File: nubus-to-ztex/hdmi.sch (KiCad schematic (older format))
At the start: 7 parts, among them J5 HDMI_A, U5 TPD12S016PWR

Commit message: large update
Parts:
- U5: URL (none) -> https://lcsc.com/product-detail/Interface-Specialized_Texas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
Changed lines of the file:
@@
 $Descr A4 11693 8268
 encoding utf-8
-Sheet 5 7
+Sheet 4 7
 Title "sbus-to-ztex blinkey stuff"
 Date ""
@@
 F 7 "IPC 7351B" H 3300 2700 50  0001 L BNN "STANDARD"
 F 8 "TPD12S016PWR" H 3300 2700 50  0001 C CNN "MPN"
+F 9 "https://lcsc.com/product-detail/Interface-Specialized_Texas-Instruments-TPD12S016PWR_C201665.html" H 3300 2700 50  0001 C CNN "URL"
 	1    3300 2700
 	1    0    0    -1

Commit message: large clean-up update
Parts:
- renumbered C21 to C20, C8 to C21, C4 to C22, C6 to C23, C7 to C24, U5 to U9
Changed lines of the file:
@@
 encoding utf-8
 Sheet 4 7
-Title "sbus-to-ztex blinkey stuff"
+Title "nubus-to-ztex HDMI"
 Date ""
 Rev ""
@@
 $EndDescr
 $Comp
-L TPD12S016PWR:TPD12S016PWR U5
+L TPD12S016PWR:TPD12S016PWR U9
 U 1 1 6148D344
 P 3300 2700
-F 0 "U5" H 3300 4067 50  0000 C CNN
+F 0 "U9" H 3300 4067 50  0000 C CNN
 F 1 "TPD12S016PWR" H 3300 3976 50  0000 C CNN
 F 2 "For_SeeedStudio:SOP65P640X120-24N" H 3300 2700 50  0001 L BNN
@@
 	4000 3800 4000 3900
 $Comp
-L power:GND #PWR0111
+L power:GND #PWR099
 U 1 1 60DDF342
 P 4000 3900
-F 0 "#PWR0111" H 4000 3650 50  0001 C CNN
+F 0 "#PWR099" H 4000 3650 50  0001 C CNN
 F 1 "GND" H 4005 3727 50  0000 C CNN
 F 2 "" H 4000 3900 50  0001 C CNN
@@
 P 4650 1300
 AR Path="/5F679B53/6148D345" Ref="C?"  Part="1"
-AR Path="/5F6B165A/6148D345" Ref="C7"  Part="1"
-AR Path="/612D28DD/6148D345" Ref="C18"  Part="1"
-AR Path="/61B62C00/6148D345" Ref="C15"  Part="1"
-F 0 "C15" H 4675 1400 50  0000 L CNN
+AR Path="/5F6B165A/6148D345" Ref="C?"  Part="1"
+AR Path="/612D28DD/6148D345" Ref="C?"  Part="1"
+AR Path="/61B62C00/6148D345" Ref="C24"  Part="1"
+F 0 "C24" H 4675 1400 50  0000 L CNN
 F 1 "100nF" H 4675 1200 50  0000 L CNN
 F 2 "Capacitor_SMD:C_0603_1608Metric" H 4688 1150 50  0001 C CNN
@@
 $EndComp
 $Comp
-L power:GND #PWR0112
+L power:GND #PWR0100
 U 1 1 6148D346
 P 4650 1450
-F 0 "#PWR0112" H 4650 1200 50  0001 C CNN
+F 0 "#PWR0100" H 4650 1200 50  0001 C CNN
 F 1 "GND" H 4655 1277 50  0000 C CNN
 F 2 "" H 4650 1450 50  0001 C CNN
@@
 $EndComp
 $Comp
-L power:+3V3 #PWR0113
+L power:+3V3 #PWR097
 U 1 1 6148D347
 P 2600 1600
-F 0 "#PWR0113" H 2600 1450 50  0001 C CNN
+F 0 "#PWR097" H 2600 1450 50  0001 C CNN
 F 1 "+3V3" H 2615 1773 50  0000 C CNN
 F 2 "" H 2600 1600 50  0001 C CNN
@@
 $EndComp
 $Comp
-L power:+5V #PWR0173
+L power:+5V #PWR098
 U 1 1 6148D348
 P 2600 1900
-F 0 "#PWR0173" H 2600 1750 50  0001 C CNN
+F 0 "#PWR098" H 2600 1750 50  0001 C CNN
 F 1 "+5V" H 2615 2073 50  0000 C CNN
 F 2 "" H 2600 1900 50  0001 C CNN
@@
 P 2250 1600
 AR Path="/5F679B53/6148D349" Ref="C?"  Part="1"
-AR Path="/5F6B165A/6148D349" Ref="C4"  Part="1"
-AR Path="/612D28DD/6148D349" Ref="C16"  Part="1"
-AR Path="/61B62C00/6148D349" Ref="C13"  Part="1"
-F 0 "C13" H 2275 1700 50  0000 L CNN
+AR Path="/5F6B165A/6148D349" Ref="C?"  Part="1"
+AR Path="/612D28DD/6148D349" Ref="C?"  Part="1"
+AR Path="/61B62C00/6148D349" Ref="C22"  Part="1"
+F 0 "C22" H 2275 1700 50  0000 L CNN
 F 1 "100nF" H 2275 1500 50  0000 L CNN
 F 2 "Capacitor_SMD:C_0603_1608Metric" H 2288 1450 50  0001 C CNN
@@
 $EndComp
 $Comp
-L power:GND #PWR0174
+L power:GND #PWR096
 U 1 1 6148D34A
 P 2100 1600
-F 0 "#PWR0174" H 2100 1350 50  0001 C CNN
+F 0 "#PWR096" H 2100 1350 50  0001 C CNN
 F 1 "GND" V 2105 1472 50  0000 R CNN
 F 2 "" H 2100 1600 50  0001 C CNN
@@
 P 2450 1900
 AR Path="/5F679B53/6148D34B" Ref="C?"  Part="1"
-AR Path="/5F6B165A/6148D34B" Ref="C6"  Part="1"
-AR Path="/612D28DD/6148D34B" Ref="C17"  Part="1"
-AR Path="/61B62C00/6148D34B" Ref="C14"  Part="1"
-F 0 "C14" H 2475 2000 50  0000 L CNN
+AR Path="/5F6B165A/6148D34B" Ref="C?"  Part="1"
+AR Path="/612D28DD/6148D34B" Ref="C?"  Part="1"
+AR Path="/61B62C00/6148D34B" Ref="C23"  Part="1"
+F 0 "C23" H 2475 2000 50  0000 L CNN
 F 1 "100nF" H 2475 1800 50  0000 L CNN
 F 2 "Capacitor_SMD:C_0603_1608Metric" H 2488 1750 50  0001 C CNN
@@
 P 2250 1350
 AR Path="/5F69F4EF/6148D34D" Ref="C?"  Part="1"
-AR Path="/5F6B165A/6148D34D" Ref="C8"  Part="1"
-AR Path="/612D28DD/6148D34D" Ref="C15"  Part="1"
-AR Path="/61B62C00/6148D34D" Ref="C12"  Part="1"
-F 0 "C12" H 2275 1450 50  0000 L CNN
+AR Path="/5F6B165A/6148D34D" Ref="C?"  Part="1"
+AR Path="/612D28DD/6148D34D" Ref="C?"  Part="1"
+AR Path="/61B62C00/6148D34D" Ref="C21"  Part="1"
+F 0 "C21" H 2275 1450 50  0000 L CNN
 F 1 "47uF 10V+" H 2275 1250 50  0000 L CNN
 F 2 "Capacitor_SMD:C_0805_2012Metric" H 2288 1200 50  0001 C CNN
@@
 AR Path="/5F6B165A/61B9B186" Ref="C?"  Part="1"
 AR Path="/612D28DD/61B9B186" Ref="C?"  Part="1"
-AR Path="/61B62C00/61B9B186" Ref="C21"  Part="1"
-F 0 "C21" H 2275 1200 50  0000 L CNN
+AR Path="/61B62C00/61B9B186" Ref="C20"  Part="1"
+F 0 "C20" H 2275 1200 50  0000 L CNN
 F 1 "10nF" H 2275 1000 50  0000 L CNN
 F 2 "Capacitor_SMD:C_0603_1608Metric" H 2288 950 50  0001 C CNN

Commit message: some missing stuff, minor HW update, SW
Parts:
- J5: URL https://www2.mouser.com/ProductDetail/Amphenol-FCI/10029449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 -> https://lcsc.com/product-detail/D-Sub-DVI-HDMI-Connectors_A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; URL-ALT (none) -> https://www2.mouser.com/ProductDetail/Amphenol-FCI/10029449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
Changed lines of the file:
@@
 F 3 "https://en.wikipedia.org/wiki/HDMI" H 6675 2550 50  0001 C CNN
 F 4 "10029449-111" H 6650 2550 50  0001 C CNN "MPN"
-F 5 "https://www2.mouser.com/ProductDetail/Amphenol-FCI/10029449-111RLF?qs=fmpTyLOWOey0HPdD9%2F%2FaXA%3D%3D" H 6650 2550 50  0001 C CNN "URL"
+F 5 "https://www2.mouser.com/ProductDetail/Amphenol-FCI/10029449-111RLF?qs=fmpTyLOWOey0HPdD9%2F%2FaXA%3D%3D" H 6650 2550 50  0001 C CNN "URL-ALT"
+F 6 "https://lcsc.com/product-detail/D-Sub-DVI-HDMI-Connectors_Amphenol-ICC-10029449-111RLF_C427307.html" H 6650 2550 50  0001 C CNN "URL"
 	1    6650 2550
 	1    0    0    -1

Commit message: cleanups, alternative MPN for 2x32 headers (TBC)
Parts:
- J5: MPN 10029449-111 -> 10029449-111RLF
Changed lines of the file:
@@
 F 2 "For_SeeedStudio:HDMI_A_Amphenol_10029449-111" H 6675 2550 50  0001 C CNN
 F 3 "https://en.wikipedia.org/wiki/HDMI" H 6675 2550 50  0001 C CNN
-F 4 "10029449-111" H 6650 2550 50  0001 C CNN "MPN"
+F 4 "10029449-111RLF" H 6650 2550 50  0001 C CNN "MPN"
 F 5 "https://www2.mouser.com/ProductDetail/Amphenol-FCI/10029449-111RLF?qs=fmpTyLOWOey0HPdD9%2F%2FaXA%3D%3D" H 6650 2550 50  0001 C CNN "URL-ALT"
 F 6 "https://lcsc.com/product-detail/D-Sub-DVI-HDMI-Connectors_Amphenol-ICC-10029449-111RLF_C427307.html" H 6650 2550 50  0001 C CNN "URL"

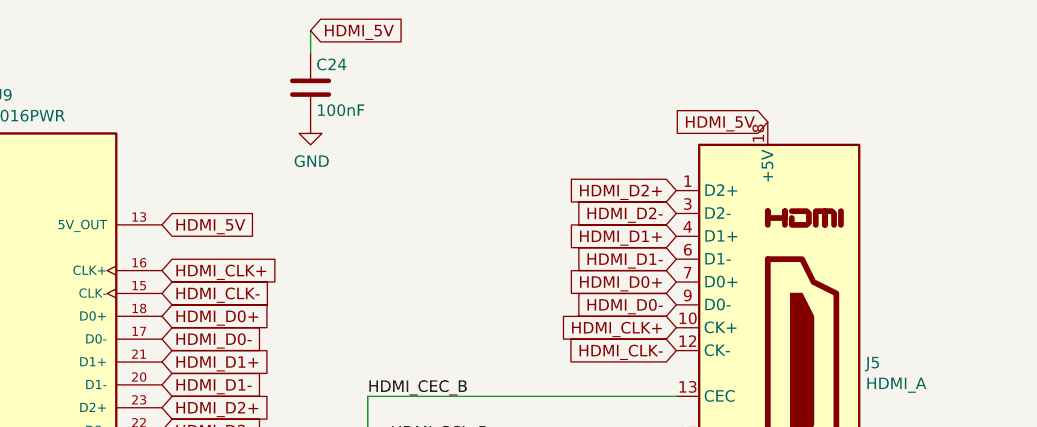
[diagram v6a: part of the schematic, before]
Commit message: merge pmod & leds into an extended pmod on the outside. Also some BoM updates.
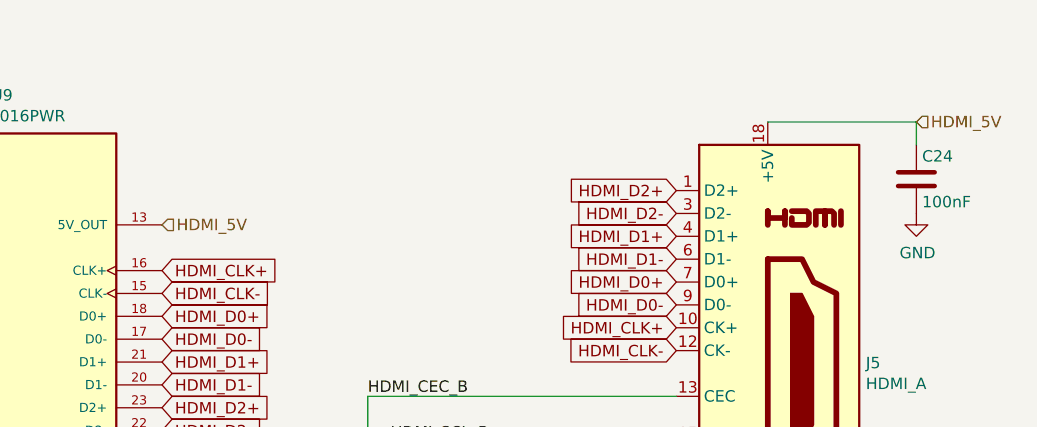
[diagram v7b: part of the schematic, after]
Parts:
- C21: MPN C2012X5R1A476MTJ00E -> GRM21BR61A476ME15K; URL https://lcsc.com/product-detail/Multilayer-Ceramic-Capacito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 -> https://www.lcsc.com/product-detail/Multilayer-Ceramic-Capa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; URL-ALT (none) -> https://lcsc.com/product-detail/Multilayer-Ceramic-Capacito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
- C23, C24: URL (none) -> https://lcsc.com/product-detail/Multilayer-Ceramic-Capacito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
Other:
- moved on the sheet: C24
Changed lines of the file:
@@
 $Descr A4 11693 8268
 encoding utf-8
-Sheet 4 10
+Sheet 4 9
 Title "nubus-to-ztex HDMI"
 Date ""
@@
 Wire Wire Line
 	4000 3650 4000 3700
-Text GLabel 6650 1450 0    50   Input ~ 0
-HDMI_5V
-Text GLabel 4000 1900 2    50   Input ~ 0
-HDMI_5V
-Text GLabel 4650 1050 2    50   Input ~ 0
-HDMI_5V
-Wire Wire Line
-	4650 1050 4650 1150
+Wire Wire Line
+	7300 1450 7300 1550
 $Comp
 L Device:C C?
 U 1 1 6148D345
-P 4650 1300
+P 7300 1700
 AR Path="/5F679B53/6148D345" Ref="C?"  Part="1"
 AR Path="/5F6B165A/6148D345" Ref="C?"  Part="1"
 AR Path="/612D28DD/6148D345" Ref="C?"  Part="1"
 AR Path="/61B62C00/6148D345" Ref="C24"  Part="1"
-F 0 "C24" H 4675 1400 50  0000 L CNN
-F 1 "100nF" H 4675 1200 50  0000 L CNN
-F 2 "Capacitor_SMD:C_0603_1608Metric" H 4688 1150 50  0001 C CNN
-F 3 "" H 4650 1300 50  0000 C CNN
-F 4 "www.yageo.com" H 4650 1300 50  0001 C CNN "MNF1_URL"
-F 5 "CC0603KRX7R8BB104" H 4650 1300 50  0001 C CNN "MPN"
-F 6 "603-CC603KRX7R8BB104" H 4650 1300 50  0001 C CNN "Mouser"
-F 7 "?" H 4650 1300 50  0001 C CNN "Digikey"
-F 8 "?" H 4650 1300 50  0001 C CNN "LCSC"
-F 9 "?" H 4650 1300 50  0001 C CNN "Koncar"
-F 10 "TB" H 4650 1300 50  0001 C CNN "Side"
-	1    4650 1300
+F 0 "C24" H 7325 1800 50  0000 L CNN
+F 1 "100nF" H 7325 1600 50  0000 L CNN
+F 2 "Capacitor_SMD:C_0603_1608Metric" H 7338 1550 50  0001 C CNN
+F 3 "" H 7300 1700 50  0000 C CNN
+F 4 "www.yageo.com" H 7300 1700 50  0001 C CNN "MNF1_URL"
+F 5 "CC0603KRX7R8BB104" H 7300 1700 50  0001 C CNN "MPN"
+F 6 "603-CC603KRX7R8BB104" H 7300 1700 50  0001 C CNN "Mouser"
+F 7 "?" H 7300 1700 50  0001 C CNN "Digikey"
+F 8 "?" H 7300 1700 50  0001 C CNN "LCSC"
+F 9 "?" H 7300 1700 50  0001 C CNN "Koncar"
+F 10 "TB" H 7300 1700 50  0001 C CNN "Side"
+F 11 "https://lcsc.com/product-detail/Multilayer-Ceramic-Capacitors-MLCC-SMD-SMT_YAGEO-CC0603KRX7R8BB104_C92490.html" H 3000 6050 50  0001 C CNN "URL"
+	1    7300 1700
 	1    0    0    -1
 $EndComp
@@
 L power:GND #PWR0100
 U 1 1 6148D346
-P 4650 1450
-F 0 "#PWR0100" H 4650 1200 50  0001 C CNN
-F 1 "GND" H 4655 1277 50  0000 C CNN
-F 2 "" H 4650 1450 50  0001 C CNN
-F 3 "" H 4650 1450 50  0001 C CNN
-	1    4650 1450
+P 7300 1850
+F 0 "#PWR0100" H 7300 1600 50  0001 C CNN
+F 1 "GND" H 7305 1677 50  0000 C CNN
+F 2 "" H 7300 1850 50  0001 C CNN
+F 3 "" H 7300 1850 50  0001 C CNN
+	1    7300 1850
 	1    0    0    -1
 $EndComp
@@
 F 9 "?" H 2450 1900 50  0001 C CNN "Koncar"
 F 10 "TB" H 2450 1900 50  0001 C CNN "Side"
+F 11 "https://lcsc.com/product-detail/Multilayer-Ceramic-Capacitors-MLCC-SMD-SMT_YAGEO-CC0603KRX7R8BB104_C92490.html" H 3000 6050 50  0001 C CNN "URL"
 	1    2450 1900
 	0    1    1    0
@@
 F 8 "https://www2.mouser.com/ProductDetail/Murata/GRM21BR60J476ME15L?qs=Tw3AuTVwGeLlkNhaDtjM1w%3D%3D" H 2250 1350 50  0001 C CNN "URL-ALT2"
 F 9 "https://www2.mouser.com/ProductDetail/?qs=u16ybLDytRYYQtTToF3RWA%3D%3D" H 2250 1350 50  0001 C CNN "URL-PREV"
-F 10 "C2012X5R1A476MTJ00E" H 2250 1350 50  0001 C CNN "MPN"
-F 11 "https://lcsc.com/product-detail/Multilayer-Ceramic-Capacitors-MLCC-SMD-SMT_TDK-C2012X5R1A476MTJ00E_C76636.html" H 2250 1350 50  0001 C CNN "URL"
+F 10 "https://lcsc.com/product-detail/Multilayer-Ceramic-Capacitors-MLCC-SMD-SMT_TDK-C2012X5R1A476MTJ00E_C76636.html" H 2250 1350 50  0001 C CNN "URL-ALT"
+F 11 "GRM21BR61A476ME15K" H 2250 1350 50  0001 C CNN "MPN"
+F 12 "https://www.lcsc.com/product-detail/Multilayer-Ceramic-Capacitors-MLCC-SMD-SMT_Murata-Electronics-GRM21BR61A476ME15K_C2292827.html" H 2250 1350 50  0001 C CNN "URL"
 	1    2250 1350
 	0    1    1    0
@@
 	4000 3650 6450 3650
 NoConn ~ 6250 3150
+Wire Wire Line
+	6650 1450 7300 1450
+Text HLabel 7300 1450 2    50   Input ~ 0
+HDMI_5V
+Text HLabel 4000 1900 2    50   Input ~ 0
+HDMI_5V
 $EndSCHEMATC

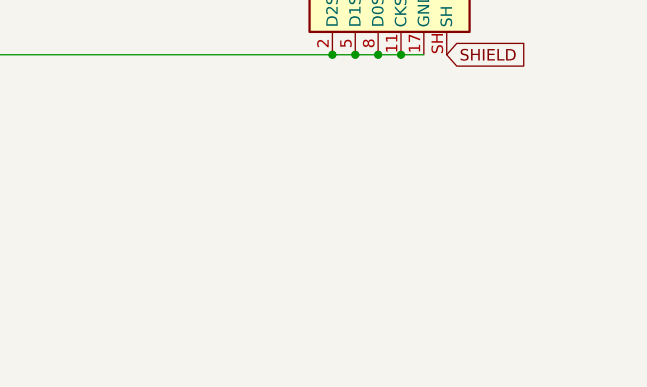
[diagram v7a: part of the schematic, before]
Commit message: move shielding to hdmi, trace cleanup
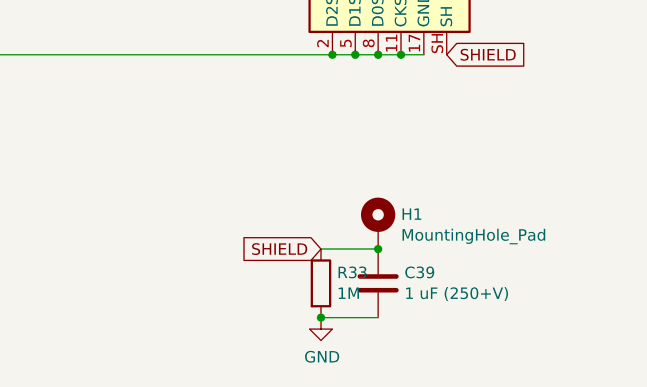
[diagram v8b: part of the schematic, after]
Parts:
- added C39: 1 uF (250+V), Capacitor_THT:CP_Radial_D6.3mm_P2.50mm, symbol Device:C
- added H1: MountingHole_Pad, MountingHole:MountingHole_2.2mm_M2_Pad, symbol Mechanical:MountingHole_Pad
- added R33: 1M, Resistor_SMD:R_1210_3225Metric, symbol Device:R
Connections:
- net GND: now also C39.2, R33.2
- net SHIELD: now also C39.1, H1.1, R33.1
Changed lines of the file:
@@
 $Descr A4 11693 8268
 encoding utf-8
-Sheet 4 9
+Sheet 4 8
 Title "nubus-to-ztex HDMI"
 Date ""
@@
 Text HLabel 4000 1900 2    50   Input ~ 0
 HDMI_5V
+Text GLabel 6400 4500 0    50   Input ~ 0
+SHIELD
+$Comp
+L power:GND #PWR?
+U 1 1 63467FDF
+P 6400 4800
+AR Path="/6193AB43/63467FDF" Ref="#PWR?"  Part="1"
+AR Path="/61B62C00/63467FDF" Ref="#PWR0132"  Part="1"
+F 0 "#PWR0132" H 6400 4550 50  0001 C CNN
+F 1 "GND" H 6405 4627 50  0000 C CNN
+F 2 "" H 6400 4800 50  0001 C CNN
+F 3 "" H 6400 4800 50  0001 C CNN
+	1    6400 4800
+	1    0    0    -1
+$EndComp
+Wire Wire Line
+	6650 4800 6400 4800
+Wire Wire Line
+	6650 4500 6400 4500
+$Comp
+L Device:C C?
+U 1 1 63467FEB
+P 6650 4650
+AR Path="/6193AB43/63467FEB" Ref="C?"  Part="1"
+AR Path="/61B62C00/63467FEB" Ref="C39"  Part="1"
+F 0 "C39" H 6765 4696 50  0000 L CNN
+F 1 "1 uF (250+V)" H 6765 4605 50  0000 L CNN
+F 2 "Capacitor_THT:CP_Radial_D6.3mm_P2.50mm" H 6688 4500 50  0001 C CNN
+F 3 "~" H 6650 4650 50  0001 C CNN
+F 4 "860021373002" H 6650 4650 50  0001 C CNN "MPN-ALT"
+F 5 "https://www2.mouser.com/ProductDetail/Wurth-Elektronik/860021373002?qs=0KOYDY2FL28tNXbPyU6hsg%3D%3D" H 6650 4650 50  0001 C CNN "URL-ALT"
+F 6 "KM010M400E110A" H 6650 4650 50  0001 C CNN "MPN"
+F 7 "https://lcsc.com/product-detail/Aluminum-Electrolytic-Capacitors-Leaded_Capxon-International-Elec-KM010M400E110A_C59365.html" H 6650 4650 50  0001 C CNN "URL"
+	1    6650 4650
+	1    0    0    -1
+$EndComp
+Connection ~ 6400 4800
+$Comp
+L Device:R R?
+U 1 1 63467FF7
+P 6400 4650
+AR Path="/6193AB43/63467FF7" Ref="R?"  Part="1"
+AR Path="/61B62C00/63467FF7" Ref="R33"  Part="1"
+F 0 "R33" H 6470 4696 50  0000 L CNN
+F 1 "1M" H 6470 4605 50  0000 L CNN
+F 2 "Resistor_SMD:R_1210_3225Metric" V 6330 4650 50  0001 C CNN
+F 3 "~" H 6400 4650 50  0001 C CNN
+F 4 "RC1210FR-071ML" H 6400 4650 50  0001 C CNN "MPN-ALT"
+F 5 "https://lcsc.com/product-detail/Chip-Resistor-Surface-Mount_YAGEO-RC1210FR-071ML_C470029.html" H 6400 4650 50  0001 C CNN "URL-ALT"
+F 6 "1210W2F1004T5E" H 6400 4650 50  0001 C CNN "MPN"
+F 7 "https://www.lcsc.com/product-detail/Chip-Resistor-Surface-Mount_UNI-ROYAL-Uniroyal-Elec-1210W2F1004T5E_C620664.html" H 6400 4650 50  0001 C CNN "URL"
+	1    6400 4650
+	1    0    0    -1
+$EndComp
+$Comp
+L Mechanical:MountingHole_Pad H?
+U 1 1 63467FFE
+P 6650 4400
+AR Path="/6193AB43/63467FFE" Ref="H?"  Part="1"
+AR Path="/61B62C00/63467FFE" Ref="H1"  Part="1"
+F 0 "H1" H 6750 4451 50  0000 L CNN
+F 1 "MountingHole_Pad" H 6750 4360 50  0000 L CNN
+F 2 "MountingHole:MountingHole_2.2mm_M2_Pad" H 6650 4400 50  0001 C CNN
+F 3 "~" H 6650 4400 50  0001 C CNN
+	1    6650 4400
+	1    0    0    -1
+$EndComp
+Connection ~ 6650 4500
 $EndSCHEMATC
